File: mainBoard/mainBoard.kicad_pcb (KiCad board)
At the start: 2 copper layers, 32 parts, among them J1 Conn_01x01, J2 Conn_01x06_Male, J3 Conn_01x06_Male, J4 Conn_01x08_Female, Q1 SS8050-G, Q2 SS8050-G, SW1 SW_Push, SW2 SW_Push, U1 AMS1117-3.3, U2 ESP32-WROOM-E

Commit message: new connector board
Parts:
- removed D3: BAT760-7, Diode_SMD:D_SOD-323F
- removed D4: LESD8D3.3CAT5G, SOD882:SOD882
- removed D5: LESD8D12T5G, SOD882:SOD882
- J2, J3: footprint Connector_JST:JST_XH_S6B-XH-A_1x06_P2.50mm_Horizontal -> Connector_JST:JST_GH_SM06B-GHS-TB_1x06-1MP_P1.25mm_Horizontal
- J4: value Conn_01x08_Female -> Conn_01x03_Male; footprint Connector_PinSocket_2.54mm:PinSocket_1x08_P2.54mm_Horizontal -> Connector_JST:JST_GH_SM03B-GHS-TB_1x03-1MP_P1.25mm_Horizontal
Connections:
- J4 pad 1: unconnected-(J4-Pad1) -> VCC
- J4 pad 2: unconnected-(J4-Pad2) -> /C-Data
- J4 pad 3: unconnected-(J4-Pad3) -> GND

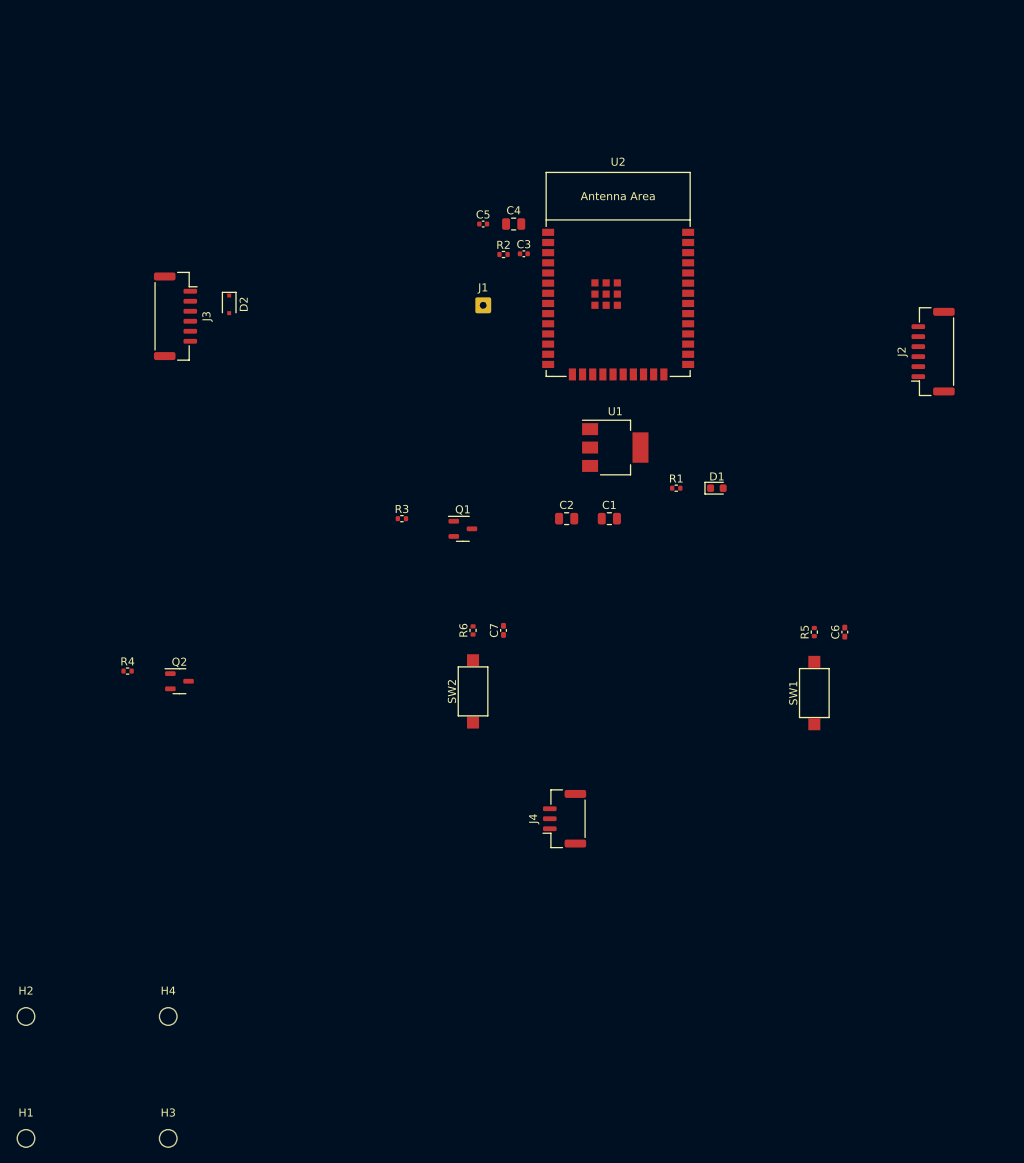
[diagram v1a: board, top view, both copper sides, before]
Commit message: main pcb rough alignment
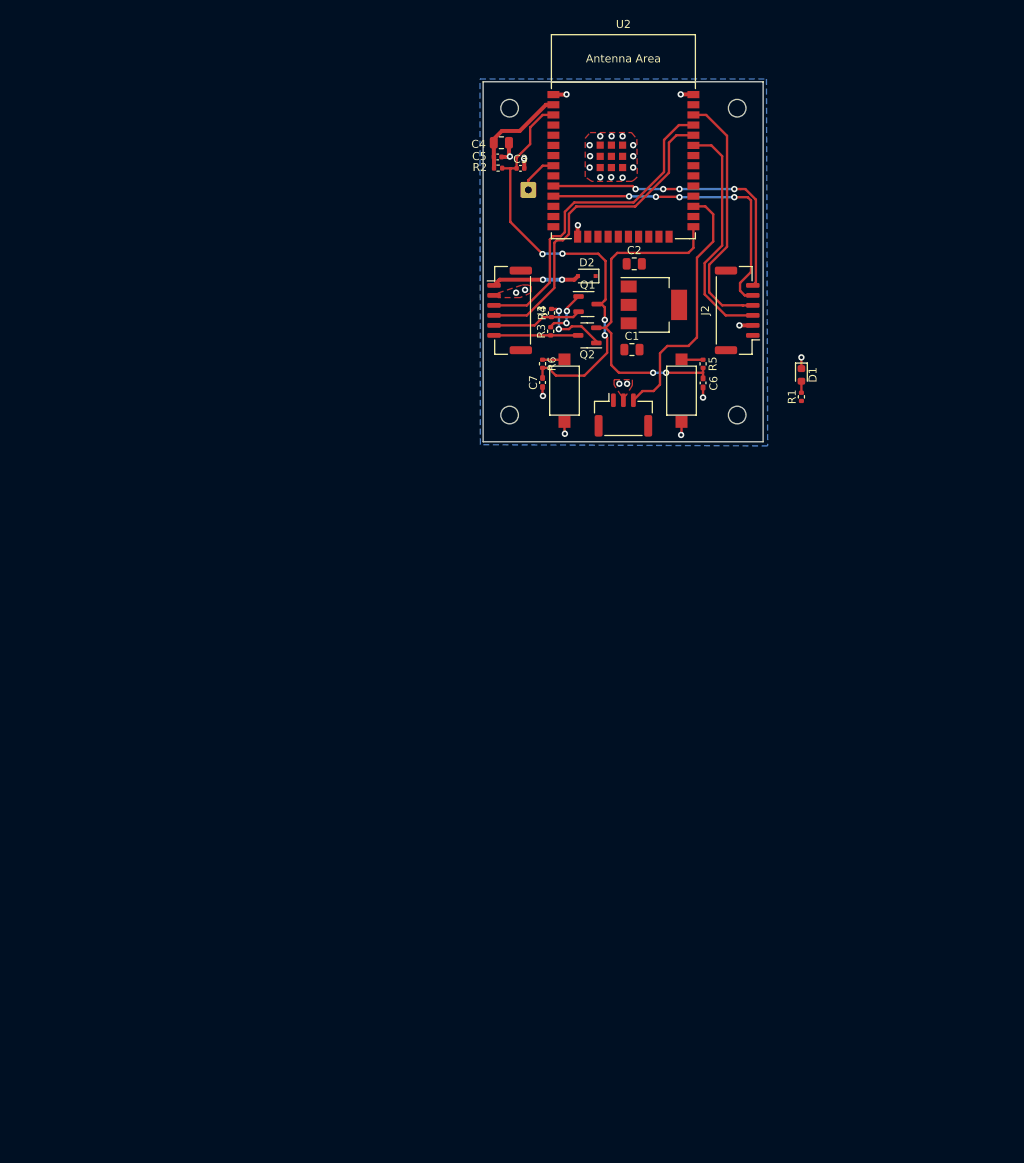
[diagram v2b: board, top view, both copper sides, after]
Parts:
- J2, J3: footprint Connector_JST:JST_GH_SM06B-GHS-TB_1x06-1MP_P1.25mm_Horizontal -> Connector_JST:JST_GH_BM06B-GHS-TBT_1x06-1MP_P1.25mm_Vertical
- moved H3 147.1 mm to (111.8, 59.2)
- moved H1 142.3 mm to (83.3, 59.2)
- moved H4 103.5 mm to (111.8, 97.5)
- moved H2 96.5 mm to (83.3, 97.5)
- moved R4 69.4 mm to (88.5, 84.8), turned to 90 degrees
- moved Q2 66.8 mm to (93.0, 87.6), turned to 180 degrees
- moved J4 51.0 mm to (97.5, 97.5), turned to 0 degrees
- moved D2 44.8 mm to (93.0, 80.2), turned to 180 degrees
- moved J3 41.8 mm to (83.3, 84.5)
- moved SW1 41.3 mm to (104.8, 94.5)
- moved SW2 39.3 mm to (90.2, 94.5)
- moved R5 36.3 mm to (107.5, 91.1), turned to -90 degrees
- moved C6 35.8 mm to (107.5, 93.5)
- moved R6 34.4 mm to (87.4, 91.1), turned to -90 degrees
- moved C2 33.0 mm to (98.9, 78.6)
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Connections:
- D2 pad 2: VCC -> Net-(D2-Pad2)
- J3 pad 1: VCC -> Net-(D2-Pad2)
- J4 pad 2: /C-Data -> GND
- J4 pad 3: GND -> /C-Data
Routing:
- net /EN: track 0.00 -> 55.9 mm, vias 0 -> 4
- net /Boot: track 0.00 -> 41.7 mm, vias 0 -> 2
- net /PR_RX: track 0.00 -> 41.3 mm
- net /PR_TX: track 0.00 -> 41.2 mm
- net /Btn_L: track 0.00 -> 38.6 mm, vias 0 -> 4
- net /Btn_R: track 0.00 -> 36.9 mm, vias 0 -> 4
- net /C-Data: track 0.00 -> 32.6 mm
- net /SCK: track 0.00 -> 31.9 mm
- net /SDA: track 0.00 -> 29.4 mm
- net GND: track 0.00 -> 17.4 mm, vias 0 -> 27
- net +3.3V: track 0.00 -> 12.9 mm
- net /CTS: track 0.00 -> 11.3 mm
- net Net-(D2-Pad2): track 0.00 -> 11.0 mm, vias 0 -> 2
- net /DTR: track 0.00 -> 10.5 mm
- net Net-(Q2-Pad1): track 0.00 -> 9.13 mm, vias 0 -> 2
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- added copper zone on B.Cu, net GND
- added copper zone on F.Cu, net GND
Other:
- board outline added: 35 x 45 mm

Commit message: routing mainboard done
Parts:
- moved D1 8.34 mm to (111.5, 92.8), turned to 90 degrees
- moved R1 7.56 mm to (113.2, 91.5), turned to -90 degrees
- moved C1 4.69 mm to (103.2, 88.3), turned to 180 degrees
- moved U1 2.34 mm to (103.4, 82.7), turned to 90 degrees
- moved C2 1.58 mm to (98.8, 80.2), turned to -90 degrees
- moved D2 0.46 mm to (93.0, 80.6)
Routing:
- net +3.3V: track 12.9 -> 68.0 mm, vias 0 -> 6
- net VCC: track 0.00 -> 32.9 mm, vias 0 -> 2
- net /C-Data: track 32.6 -> 38.5 mm
- net GND: track 17.4 -> 17.7 mm, vias 27 -> 32
- added copper zone on F.Cu, net +3.3V
- added copper zone on F.Cu, net VCC

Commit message: main pcb for order
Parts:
- moved H1 7.11 mm to (83.3, 52.1)
- moved H3 7.11 mm to (111.8, 52.1)
- moved R1 0.76 mm to (112.5, 91.5)
- moved C2 0.66 mm to (98.1, 80.2)
- moved D1 0.51 mm to (110.9, 92.9)
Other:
- board size 35 x 45 mm -> 35 x 52.1 mm
- board text added: "+"
- board text added: "ADC"
- board text added: "BOOT"
- board text added: "Controller"
- board text added: "EN"
- board text added: "Flash"
- board text added: "IO"
- board text added: "JLCJLCJLCJLC"
- board text added: "Mainboard v.0.9"
- board text added: "PWR"

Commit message: connector and emitter switched
maybe a problem maybe not
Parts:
- SW1, SW2: value SW_Push -> C520860
- moved Q2 0.31 mm to (92.7, 87.6), turned to 0 degrees
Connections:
- Q2 pad 2: /Boot -> /DTR
- Q2 pad 3: /DTR -> /Boot
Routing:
- net Net-(Q2-Pad1): track 9.13 -> 5.77 mm
- net /Boot: track 41.7 -> 42.6 mm
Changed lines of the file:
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@@
     (property "Sheetfile" "mainBoard.kicad_sch")
     (property "Sheetname" "")
-    (attr exclude_from_pos_files exclude_from_bom)
+    (attr exclude_from_pos_files)
     (fp_text reference "J1" (at 0 -2.286) (layer "F.Fab")
       (effects (font (size 1 1) (thickness 0.15)))
@@
     (property "Sheetfile" "mainBoard.kicad_sch")
     (property "Sheetname" "")
-    (attr exclude_from_pos_files exclude_from_bom)
+    (attr exclude_from_pos_files)
     (fp_text reference "H2" (at 0 -3.2) (layer "F.Fab")
       (effects (font (size 1 1) (thickness 0.15)))
@@
     (property "Sheetfile" "mainBoard.kicad_sch")
     (property "Sheetname" "")
-    (attr exclude_from_pos_files exclude_from_bom)
+    (attr exclude_from_pos_files)
     (fp_text reference "H1" (at 0 -3.2) (layer "F.Fab")
       (effects (font (size 1 1) (thickness 0.15)))
@@
     (property "Sheetfile" "mainBoard.kicad_sch")
     (property "Sheetname" "")
-    (attr exclude_from_pos_files exclude_from_bom)
+    (attr exclude_from_pos_files)
     (fp_text reference "H4" (at 0 -3.2) (layer "F.Fab")
       (effects (font (size 1 1) (thickness 0.15)))
@@
       (effects (font (size 1 1) (thickness 0.15)))
     )
-    (fp_text value "SW_Push" (at 0 3 90) (layer "F.Fab")
+    (fp_text value "C520860" (at 0 3 90) (layer "F.Fab")
       (effects (font (size 1 1) (thickness 0.15)))
     )
@@
   )
   (footprint "Package_TO_SOT_SMD:SOT-23-3" (layer "F.Cu")
-    (at 93.0148 87.5792 180)
+    (at 92.71 87.63)
     (descr "SOT, 3 Pin (https://www.jedec.org/sites/default/files/docs/Mo-178D.PDF inferred 3-pin variant), generated with kicad-footprint-generator ipc_gullwing_generator.py")
     (tags "SOT TO_SOT_SMD")
@@
     (fp_line (start -0.8 1.45) (end -0.8 -1.05) (layer "F.Fab") (width 0.1))
     (fp_line (start 0.8 -1.45) (end 0.8 1.45) (layer "F.Fab") (width 0.1))
-    (pad "1" smd roundrect locked (at -1.1375 -0.95 180) (size 1.325 0.6) (layers "F.Cu" "F.Paste" "F.Mask") (roundrect_rratio 0.25)
+    (pad "1" smd roundrect locked (at -1.1375 -0.95) (size 1.325 0.6) (layers "F.Cu" "F.Paste" "F.Mask") (roundrect_rratio 0.25)
       (net 18 "Net-(Q2-Pad1)") (pinfunction "B") (pintype "input"))
-    (pad "2" smd roundrect locked (at -1.1375 0.95 180) (size 1.325 0.6) (layers "F.Cu" "F.Paste" "F.Mask") (roundrect_rratio 0.25)
-      (net 5 "/Boot") (pinfunction "E") (pintype "passive"))
-    (pad "3" smd roundrect locked (at 1.1375 0 180) (size 1.325 0.6) (layers "F.Cu" "F.Paste" "F.Mask") (roundrect_rratio 0.25)
-      (net 15 "/DTR") (pinfunction "C") (pintype "passive"))
+    (pad "2" smd roundrect locked (at -1.1375 0.95) (size 1.325 0.6) (layers "F.Cu" "F.Paste" "F.Mask") (roundrect_rratio 0.25)
+      (net 15 "/DTR") (pinfunction "E") (pintype "passive"))
+    (pad "3" smd roundrect locked (at 1.1375 0) (size 1.325 0.6) (layers "F.Cu" "F.Paste" "F.Mask") (roundrect_rratio 0.25)
+      (net 5 "/Boot") (pinfunction "C") (pintype "passive"))
     (model "${KICAD6_3DMODEL_DIR}/Package_TO_SOT_SMD.3dshapes/SOT-23-3.wrl"
       (offset (xyz 0 0 0))
@@
       (effects (font (size 1 1) (thickness 0.15)))
     )
-    (fp_text value "SW_Push" (at 0 3 90) (layer "F.Fab")
+    (fp_text value "C520860" (at 0 3 90) (layer "F.Fab")
       (effects (font (size 1 1) (thickness 0.15)))
     )
@@
     (property "Sheetfile" "mainBoard.kicad_sch")
     (property "Sheetname" "")
-    (attr exclude_from_pos_files exclude_from_bom)
+    (attr exclude_from_pos_files)
     (fp_text reference "H3" (at 0 -3.2) (layer "F.Fab")
       (effects (font (size 1 1) (thickness 0.15)))
@@
   (segment (start 107.4928 92.9553) (end 107.4928 92.2528) (width 0.3) (layer "F.Cu") (net 5))
   (segment (start 95.316 86.5988) (end 96.012 85.9028) (width 0.3) (layer "F.Cu") (net 5))
+  (segment (start 93.8475 87.63) (end 93.8475 87.2545) (width 0.3) (layer "F.Cu") (net 5))
   (segment (start 105.664 77.2668) (end 106.286 76.6448) (width 0.3) (layer "F.Cu") (net 5))
   (segment (start 107.4928 92.2528) (end 101.2303 92.2528) (width 0.3) (layer "F.Cu") (net 5))
@@
   (segment (start 96.012 78.0288) (end 96.774 77.2668) (width 0.3) (layer "F.Cu") (net 5))
   (segment (start 106.286 76.6448) (end 106.286 73.992) (width 0.3) (layer "F.Cu") (net 5))
+  (segment (start 94.4728 86.6292) (end 95.316 86.6292) (width 0.3) (layer "F.Cu") (net 5))
   (segment (start 96.9772 92.2528) (end 96.012 91.2876) (width 0.3) (layer "F.Cu") (net 5))
-  (segment (start 95.316 86.6292) (end 94.1523 86.6292) (width 0.3) (layer "F.Cu") (net 5))
+  (segment (start 93.8475 87.2545) (end 94.4728 86.6292) (width 0.3) (layer "F.Cu") (net 5))
   (segment (start 96.012 91.2876) (end 96.012 87.3252) (width 0.3) (layer "F.Cu") (net 5))
   (segment (start 95.316 86.6292) (end 95.316 86.5988) (width 0.3) (layer "F.Cu") (net 5))
@@
   (segment (start 88.5444 85.2952) (end 91.2505 85.2952) (width 0.3) (layer "F.Cu") (net 14))
   (segment (start 87.4756 85.2952) (end 86.4408 86.33) (width 0.3) (layer "F.Cu") (net 14))
-  (segment (start 88.4428 87.5812) (end 88.4416 87.58) (width 0.3) (layer "F.Cu") (net 15))
-  (segment (start 88.4428 87.5812) (end 88.4448 87.5792) (width 0.3) (layer "F.Cu") (net 15))
   (segment (start 88.4416 87.58) (end 81.362 87.58) (width 0.3) (layer "F.Cu") (net 15))
-  (segment (start 88.4448 87.5792) (end 91.8773 87.5792) (width 0.3) (layer "F.Cu") (net 15))
+  (segment (start 89.342 88.58) (end 88.4428 87.6808) (width 0.3) (layer "F.Cu") (net 15))
+  (segment (start 88.4428 87.6808) (end 88.4428 87.5812) (width 0.3) (layer "F.Cu") (net 15))
+  (segment (start 89.342 88.58) (end 91.5725 88.58) (width 0.3) (layer "F.Cu") (net 15))
   (segment (start 99.6068 91.942139) (end 99.167461 91.5028) (width 0.3) (layer "F.Cu") (net 16))
   (segment (start 107.3676 71.452) (end 106.286 71.452) (width 0.3) (layer "F.Cu") (net 16))
@@
   (segment (start 90.4748 84.5457) (end 90.424 84.5965) (width 0.3) (layer "B.Cu") (net 17))
   (segment (start 90.424 84.5965) (end 90.424 86.0447) (width 0.3) (layer "B.Cu") (net 17))
-  (segment (start 91.076081 86.45328) (end 92.29528 86.45328) (width 0.3) (layer "F.Cu") (net 18))
+  (segment (start 89.7866 87.122) (end 91.186 87.122) (width 0.3) (layer "F.Cu") (net 18))
   (segment (start 89.221717 84.2752) (end 89.475438 84.528921) (width 0.3) (layer "F.Cu") (net 18))
-  (segment (start 90.734661 86.7947) (end 91.076081 86.45328) (width 0.3) (layer "F.Cu") (net 18))
-  (segment (start 92.29528 86.45328) (end 94.1523 88.3103) (width 0.3) (layer "F.Cu") (net 18))
   (segment (start 88.5444 84.2752) (end 89.221717 84.2752) (width 0.3) (layer "F.Cu") (net 18))
-  (segment (start 89.4588 86.7942) (end 89.4593 86.7947) (width 0.3) (layer "F.Cu") (net 18))
-  (segment (start 89.4593 86.7947) (end 90.734661 86.7947) (width 0.3) (layer "F.Cu") (net 18))
-  (segment (start 94.1523 88.3103) (end 94.1523 88.5292) (width 0.3) (layer "F.Cu") (net 18))
+  (segment (start 91.186 87.122) (end 91.5725 86.7355) (width 0.3) (layer "F.Cu") (net 18))
+  (segment (start 91.5725 86.7355) (end 91.5725 86.68) (width 0.3) (layer "F.Cu") (net 18))
+  (segment (start 89.4588 86.7942) (end 89.7866 87.122) (width 0.3) (layer "F.Cu") (net 18))
   (via (at 89.475438 84.528921) (size 0.8) (drill 0.4) (layers "F.Cu" "B.Cu") (net 18))
   (via (at 89.4588 86.7942) (size 0.8) (drill 0.4) (layers "F.Cu" "B.Cu") (net 18))

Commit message: cleanup
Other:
- board text added: "Mainboard v1.0"
- board text removed: "Mainboard v.0.9"
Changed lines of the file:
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@@
   )
   (paper "A4")
+  (title_block
+    (title "Mainboard")
+    (date "2023-02-14")
+    (rev "1.0")
+    (company "Fabian Kuffer")
+  )
   (layers
     (0 "F.Cu" signal)
@@
   (gr_arc (start 83.3528 100.88) (mid 80.982012 99.897988) (end 80 97.5272) (layer "Edge.Cuts") (width 0.1))
   (gr_line (start 97.9572 55.518) (end 97.9572 105.518) (layer "User.1") (width 0.15))
-  (gr_text "Mainboard\nv.0.9" (at 96.6216 77.3684) (layer "B.SilkS")
+  (gr_text "Mainboard\nv1.0" (at 96.6216 77.3684) (layer "B.SilkS")
     (effects (font (size 1 1) (thickness 0.15)) (justify mirror))
   )
